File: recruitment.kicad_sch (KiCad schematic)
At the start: 3 parts, among them K1 Relay_SPST_Latching_2coil

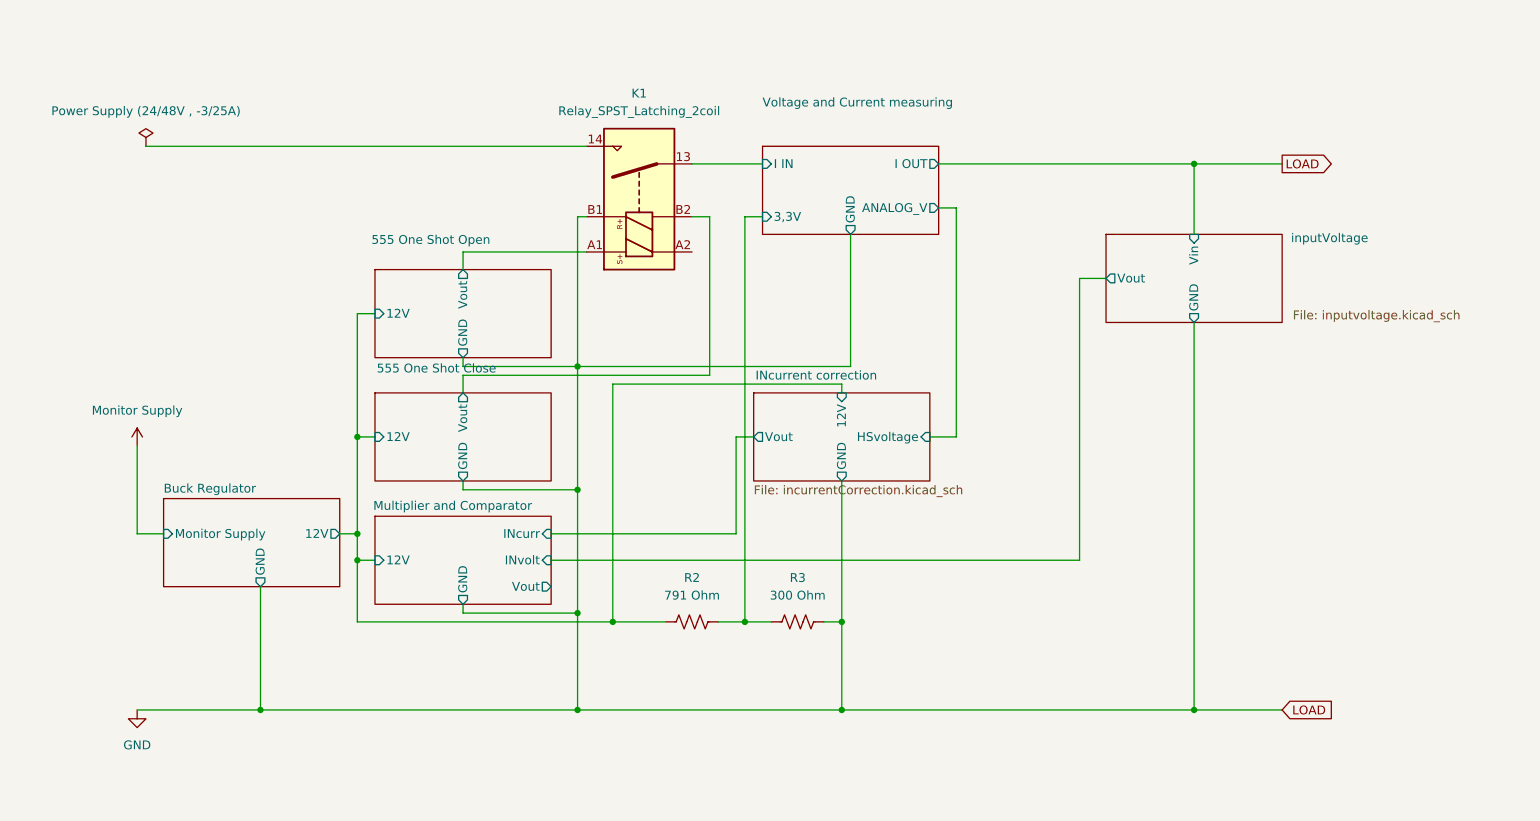
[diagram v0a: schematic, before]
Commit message: Schematic Complete
Completed the wiring of the circuit.

(Missing some labels and footprints)
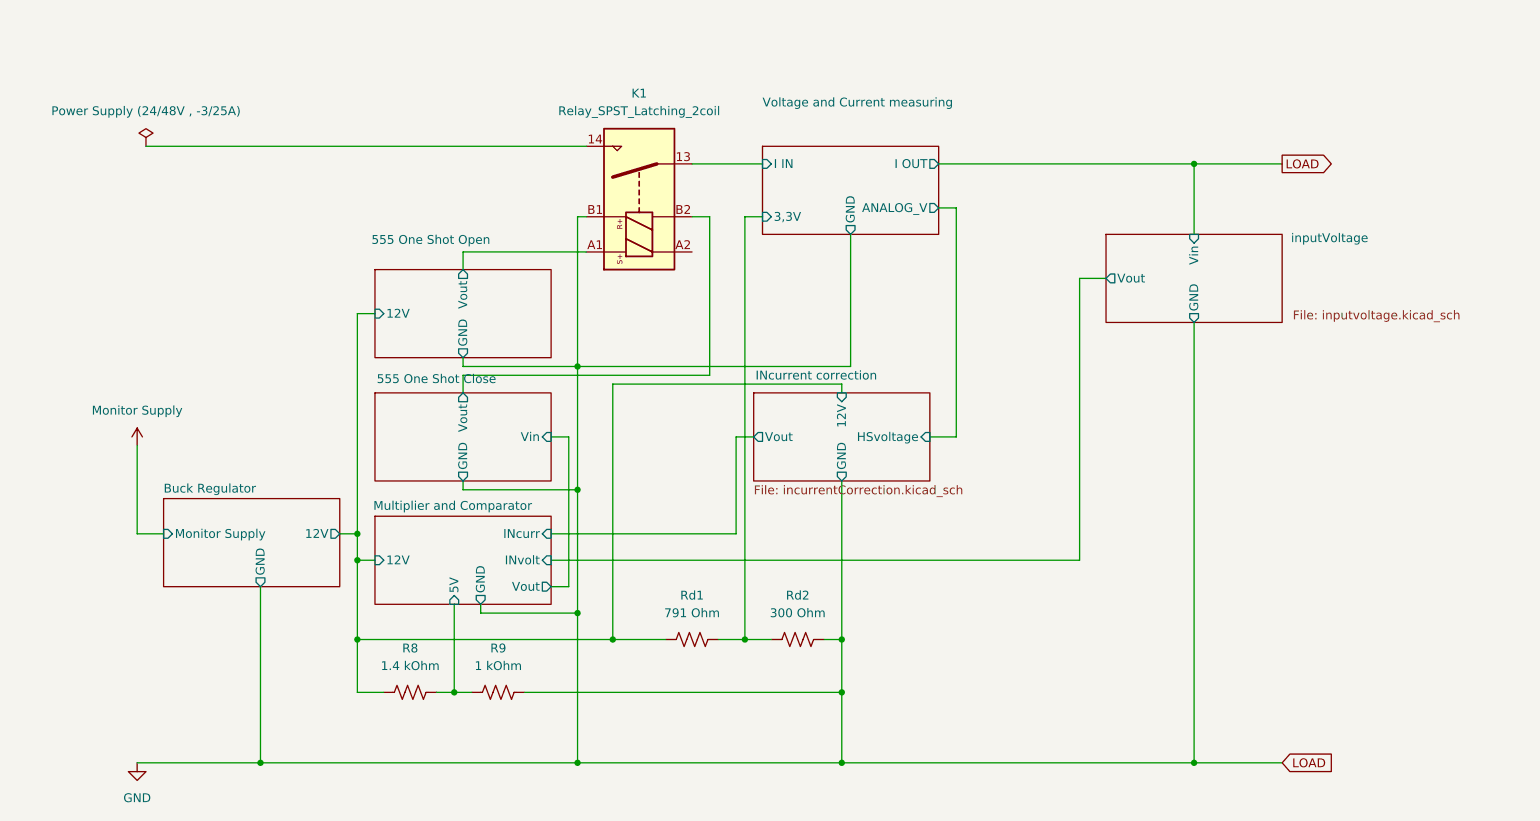
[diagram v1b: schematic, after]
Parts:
- added R8: 1.4 kOhm, symbol Device:R_US
- added R9: 1 kOhm, symbol Device:R_US
- K1: footprint (none) -> Relay_THT:Relay_SPST_Omron-G5Q-1A
- Rd2: renamed from R3; footprint (none) -> Resistor_SMD:R_0805_2012Metric_Pad1.20x1.40mm_HandSolder
- renumbered R2 to Rd1
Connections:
- net GND: now also R9.2
- net 555 One Shot Close/12V renamed 555 One Shot Open/12V
- net 555 One Shot Open/12V: now also R8.1
- new net Multiplier and Comparator/5V: R8.2, R9.1
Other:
- sheet 555 One Shot Close ports: added Vin; removed 12V
- sheet Multiplier and Comparator ports: added 5V; removed none
- moved on the sheet: Rd1, Rd2

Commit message: Finished (?)
Assigned al values, footprints and generated traces.
Generated DRL files.
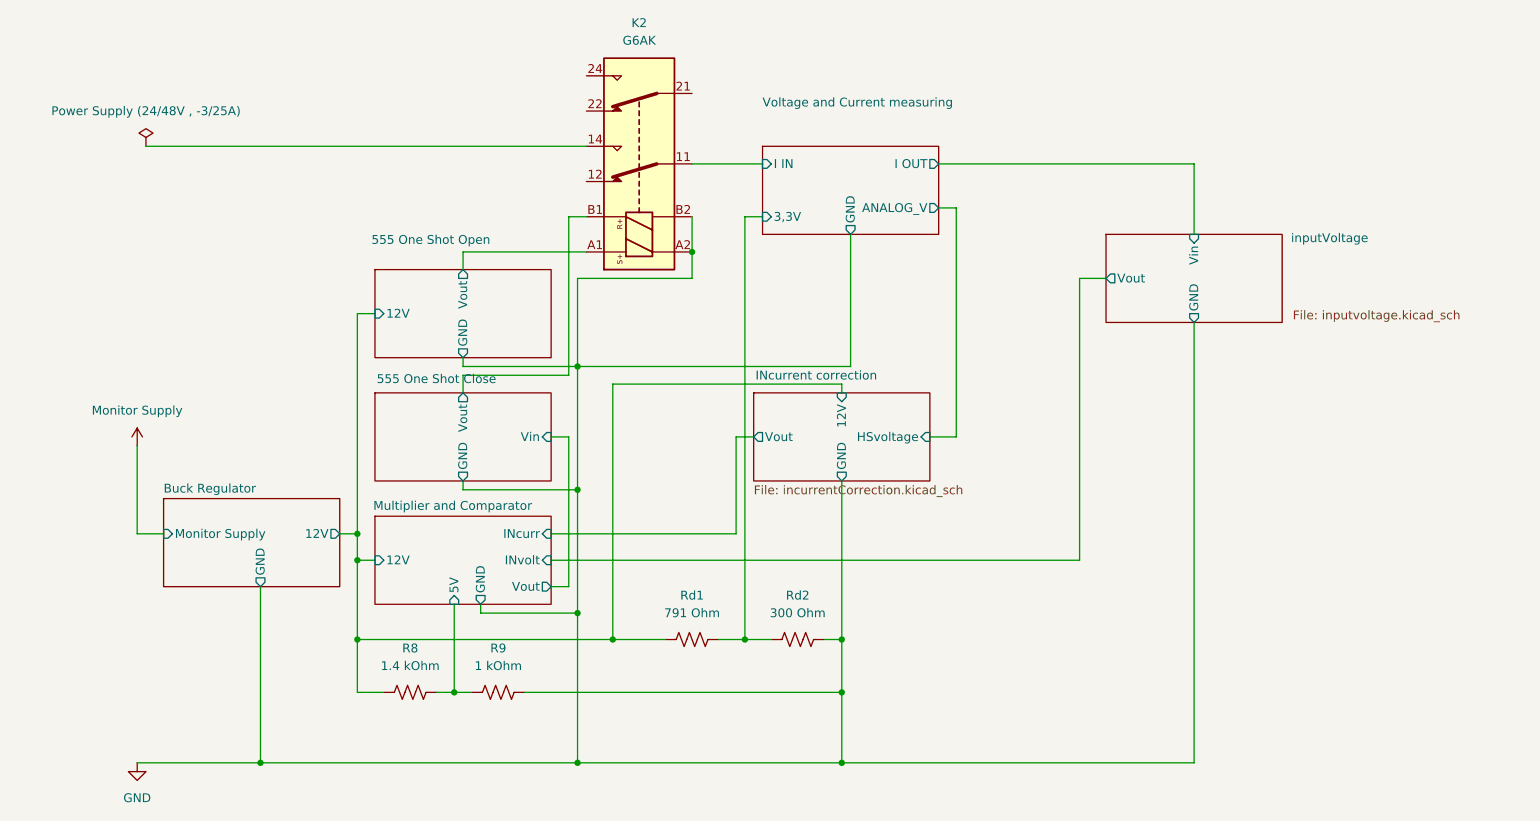
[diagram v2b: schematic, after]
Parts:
- removed K1: Relay_SPST_Latching_2coil, Relay_THT:Relay_SPST_Omron-G5Q-1A, symbol Relay:Relay_SPST_Latching_2coil
- added K2: G6AK, Relay_THT:Relay_DPDT_Omron_G6AK, symbol Relay:G6AK
- R8, Rd1: footprint (none) -> Resistor_SMD:R_0805_2012Metric
- R9: footprint (none) -> Resistor_SMD:R_1206_3216Metric_Pad1.30x1.75mm_HandSolder
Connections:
- net 555 One Shot Close/Vout: now also K2.B1
- net 555 One Shot Open/Vout: now also K2.A1
- net GND: now also K2.A2, K2.B2
- net Voltage and Current measuring/I IN: now also K2.11
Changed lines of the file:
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@@
+	)
+	(junction
+		(at 143.51 53.34)
+		(diameter 0)
+		(color 0 0 0 0)
 	)
 	(junction
@@
 	)
 	(junction
-		(at 215.9 40.64)
-		(diameter 0)
-		(color 0 0 0 0)
-	)
-	(junction
 		(at 132.08 109.22)
 		(diameter 0)
@@
 	)
 	(junction
-		(at 215.9 127)
-		(diameter 0)
-		(color 0 0 0 0)
-	)
-	(junction
 		(at 165.1 127)
 		(diameter 0)
@@
 	(wire
 		(pts
-			(xy 215.9 40.64) (xy 228.6 40.64)
-		)
-		(stroke
-			(width 0)
-			(type default)
-		)
-	)
-	(wire
-		(pts
 			(xy 181.61 80.01) (xy 177.8 80.01)
 		)
@@
 	(wire
 		(pts
+			(xy 125.73 48.26) (xy 125.73 71.12)
+		)
+		(stroke
+			(width 0)
+			(type default)
+		)
+	)
+	(wire
+		(pts
 			(xy 165.1 109.22) (xy 165.1 116.84)
 		)
@@
 	(wire
 		(pts
-			(xy 146.05 48.26) (xy 146.05 71.12)
-		)
-		(stroke
-			(width 0)
-			(type default)
-		)
-	)
-	(wire
-		(pts
 			(xy 63.5 93.98) (xy 67.31 93.98)
 		)
@@
 	(wire
 		(pts
+			(xy 125.73 48.26) (xy 128.27 48.26)
+		)
+		(stroke
+			(width 0)
+			(type default)
+		)
+	)
+	(wire
+		(pts
+			(xy 127 57.15) (xy 127 69.85)
+		)
+		(stroke
+			(width 0)
+			(type default)
+		)
+	)
+	(wire
+		(pts
 			(xy 95.25 93.98) (xy 95.25 97.79)
 		)
@@
 	(wire
 		(pts
-			(xy 127 48.26) (xy 128.27 48.26)
-		)
-		(stroke
-			(width 0)
-			(type default)
-		)
-	)
-	(wire
-		(pts
 			(xy 110.49 68.58) (xy 110.49 69.85)
 		)
@@
 	(wire
 		(pts
-			(xy 110.49 71.12) (xy 146.05 71.12)
+			(xy 110.49 71.12) (xy 125.73 71.12)
 		)
 		(stroke
@@
 	(wire
 		(pts
-			(xy 146.05 48.26) (xy 143.51 48.26)
-		)
-		(stroke
-			(width 0)
-			(type default)
-		)
-	)
-	(wire
-		(pts
-			(xy 215.9 127) (xy 228.6 127)
-		)
-		(stroke
-			(width 0)
-			(type default)
-		)
-	)
-	(wire
-		(pts
 			(xy 125.73 101.6) (xy 125.73 80.01)
 		)
@@
 	(wire
 		(pts
+			(xy 143.51 53.34) (xy 143.51 57.15)
+		)
+		(stroke
+			(width 0)
+			(type default)
+		)
+	)
+	(wire
+		(pts
+			(xy 143.51 57.15) (xy 127 57.15)
+		)
+		(stroke
+			(width 0)
+			(type default)
+		)
+	)
+	(wire
+		(pts
 			(xy 165.1 73.66) (xy 165.1 72.39)
 		)
@@
 	(wire
 		(pts
+			(xy 143.51 48.26) (xy 143.51 53.34)
+		)
+		(stroke
+			(width 0)
+			(type default)
+		)
+	)
+	(wire
+		(pts
 			(xy 203.2 57.15) (xy 199.39 57.15)
 		)
@@
 	(wire
 		(pts
-			(xy 127 48.26) (xy 127 69.85)
-		)
-		(stroke
-			(width 0)
-			(type default)
-		)
-	)
-	(wire
-		(pts
 			(xy 165.1 127) (xy 215.9 127)
 		)
@@
 			(width 0)
 			(type default)
-		)
-	)
-	(global_label "LOAD"
-		(shape input)
-		(at 228.6 127 0)
-		(fields_autoplaced yes)
-		(effects
-			(font
-				(size 1.27 1.27)
-			)
-			(justify left)
-		)
-		(property "Intersheetrefs" "${INTERSHEET_REFS}"
-			(at 235.6482 127 0)
-			(effects
-				(font
-					(size 1.27 1.27)
-				)
-				(justify left)
-				(hide yes)
-			)
-		)
-	)
-	(global_label "LOAD"
-		(shape output)
-		(at 228.6 40.64 0)
-		(fields_autoplaced yes)
-		(effects
-			(font
-				(size 1.27 1.27)
-			)
-			(justify left)
-		)
-		(property "Intersheetrefs" "${INTERSHEET_REFS}"
-			(at 235.6482 40.64 0)
-			(effects
-				(font
-					(size 1.27 1.27)
-				)
-				(justify left)
-				(hide yes)
-			)
-		)
-	)
-	(symbol
-		(lib_id "Relay:Relay_SPST_Latching_2coil")
-		(at 135.89 45.72 90)
-		(unit 1)
-		(exclude_from_sim no)
-		(in_bom yes)
-		(on_board yes)
-		(dnp no)
-		(fields_autoplaced yes)
-		(property "Reference" "K1"
-			(at 135.89 30.48 90)
-			(effects
-				(font
-					(size 1.27 1.27)
-				)
-			)
-		)
-		(property "Value" "Relay_SPST_Latching_2coil"
-			(at 135.89 33.02 90)
-			(effects
-				(font
-					(size 1.27 1.27)
-				)
-			)
-		)
-		(property "Footprint" "Relay_THT:Relay_SPST_Omron-G5Q-1A"
-			(at 137.16 12.065 0)
-			(effects
-				(font
-					(size 1.27 1.27)
-				)
-				(hide yes)
-			)
-		)
-		(property "Datasheet" "~"
-			(at 135.89 45.72 0)
-			(effects
-				(font
-					(size 1.27 1.27)
-				)
-				(justify left)
-				(hide yes)
-			)
-		)
-		(property "Description" "Relay SPST, bistable, double-coil, EN50005"
-			(at 135.89 45.72 0)
-			(effects
-				(font
-					(size 1.27 1.27)
-				)
-				(hide yes)
-			)
-		)
-		(pin "A2"
-		)
-		(pin "14"
-		)
-		(pin "A1"
-		)
-		(pin "B1"
-		)
-		(pin "B2"
-		)
-		(pin "13"
-		)
-		(instances
-			(project ""
-				(path "/bdc7face-9f7c-4701-80bb-4cc144448db1"
-					(reference "K1")
-					(unit 1)
-				)
-			)
 		)
 	)
@@
 	)
 	(symbol
+		(lib_id "Relay:G6AK")
+		(at 135.89 40.64 90)
+		(unit 1)
+		(exclude_from_sim no)
+		(in_bom yes)
+		(on_board yes)
+		(dnp no)
+		(fields_autoplaced yes)
+		(property "Reference" "K2"
+			(at 135.89 20.32 90)
+			(effects
+				(font
+					(size 1.27 1.27)
+				)
+			)
+		)
+		(property "Value" "G6AK"
+			(at 135.89 22.86 90)
+			(effects
+				(font
+					(size 1.27 1.27)
+				)
+			)
+		)
+		(property "Footprint" "Relay_THT:Relay_DPDT_Omron_G6AK"
+			(at 135.89 40.64 0)
+			(effects
+				(font
+					(size 1.27 1.27)
+				)
+				(justify left)
+				(hide yes)
+			)
+		)
+		(property "Datasheet" "https://omronfs.omron.com/en_US/ecb/products/pdf/en-g6a.pdf"
+			(at 135.89 40.64 0)
+			(effects
+				(font
+					(size 1.27 1.27)
+				)
+				(hide yes)
+			)
+		)
+		(property "Description" "Industry-Standard 2-pole relay, designed to switch 2A Signal Loads, Double-winding Latching"
+			(at 135.89 40.64 0)
+			(effects
+				(font
+					(size 1.27 1.27)
+				)
+				(hide yes)
+			)
+		)
+		(pin "A2"
+		)
+		(pin "21"
+		)
+		(pin "A1"
+		)
+		(pin "B1"
+		)
+		(pin "14"
+		)
+		(pin "22"
+		)
+		(pin "B2"
+		)
+		(pin "12"
+		)
+		(pin "11"
+		)
+		(pin "24"
+		)
+		(instances
+			(project ""
+				(path "/bdc7face-9f7c-4701-80bb-4cc144448db1"
+					(reference "K2")
+					(unit 1)
+				)
+			)
+		)
+	)
+	(symbol
 		(lib_id "Device:R_US")
 		(at 102.87 116.84 90)
@@
 			)
 		)
-		(property "Footprint" ""
+		(property "Footprint" "Resistor_SMD:R_0805_2012Metric"
 			(at 103.124 115.824 90)
 			(effects
@@
 			)
 		)
-		(property "Footprint" ""
+		(property "Footprint" "Resistor_SMD:R_1206_3216Metric_Pad1.30x1.75mm_HandSolder"
 			(at 115.824 115.824 90)
 			(effects
@@
 			)
 		)
-		(property "Footprint" ""
+		(property "Footprint" "Resistor_SMD:R_0805_2012Metric"
 			(at 143.764 108.204 90)
 			(effects
